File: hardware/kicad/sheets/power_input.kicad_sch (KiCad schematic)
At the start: 5 parts, among them J2 12V IN

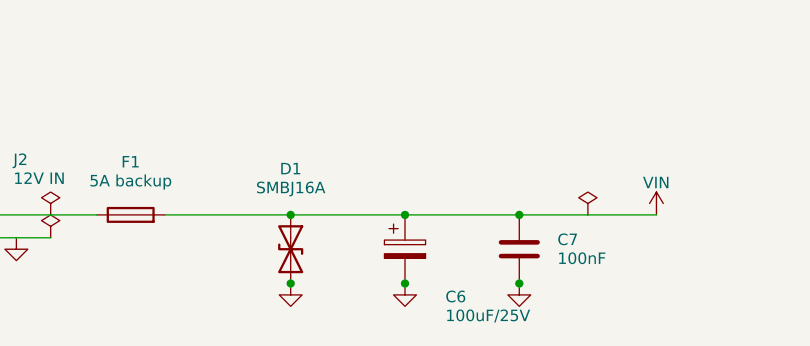
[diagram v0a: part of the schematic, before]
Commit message: KiCad: cleaner layout, decoupling blocks, label directions, KiCad format fixes
- move IC decoupling caps into labelled blocks at the side of each sheet
- global labels show input/output direction per net
- no 4-way junctions (generator now checks and fails)
- generator output matches KiCad's saved format (hide property, junction
  and wire normalisation, lib symbol embedded fonts, multi-unit pins)
- hand-laid USB ESD protection as a pass-through

Co-Authored-By: Claude Sonnet 5.5 <noreply@anthropic.com>
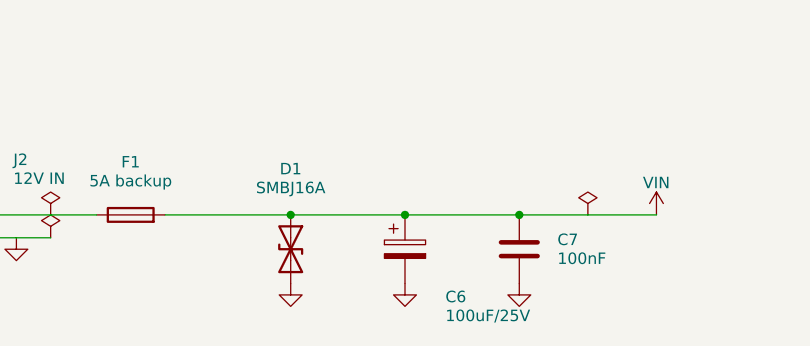
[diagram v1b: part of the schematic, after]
